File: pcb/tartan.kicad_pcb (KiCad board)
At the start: 2 copper layers, 285 x 117 mm, 165 parts, among them J1 AVR_ISP_6, J3 Conn_01x01_Pin, J4 USB_OTG, SW1 SW_Push, SW10 SW_Push, SW11 SW_Push, SW12 SW_Push, SW13 SW_Push, SW14 SW_Push, SW15 SW_Push, SW16 SW_Push, SW17 SW_Push, SW18 SW_Push, SW19 SW_Push, SW2 SW_Push, SW20 SW_Push, SW21 SW_Push, SW22 SW_Push, SW23 SW_Push, SW24 SW_Push, SW25 SW_Push, SW26 SW_Push, SW27 SW_Push, SW28 SW_Push, SW29 SW_Push, SW3 SW_Push, SW30 SW_Push, SW31 SW_Push, SW32 SW_Push, SW33 SW_Push, SW34 SW_Push, SW35 SW_Push, SW36 SW_Push, SW37 SW_Push, SW38 SW_Push, SW39 SW_Push, SW4 SW_Push, SW40 SW_Push, SW41 SW_Push, SW42 SW_Push, SW43 SW_Push, SW44 SW_Push, SW45 SW_Push, SW46 SW_Push, SW47 SW_Push, SW48 SW_Push, SW49 SW_Push, SW5 SW_Push, SW50 SW_Push, SW51 SW_Push, SW52 SW_Push, SW53 SW_Push, SW54 SW_Push, SW55 SW_Push, SW56 SW_Push, SW57 SW_Push, SW58 SW_Push, SW59 SW_Push, SW6 SW_Push, SW60 SW_Push, SW61 SW_Push, SW62 SW_Push, SW63 SW_Push, SW64 SW_Push, SW65 SW_Push, SW66 SW_Push, SW67 SW_Push, SW68 SW_Push, SW69 SW_Push, SW7 SW_Push, SW70 RESET, SW71 BOOT, SW8 SW_Push, SW9 SW_Push, U1 ATMEGA328-PU, Y1 16MHz

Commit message: Added stabilizers back and hopefully fixed a bunch of issues (tm).
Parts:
- added STAB1: 2U, tartan:STAB_MX_2u, F.Cu at (295.9, 61.1)
- added STAB2: 2U, tartan:STAB_MX_2u, F.Cu at (303.7, 90.6)
- added STAB3: 2U, tartan:STAB_MX_2u, F.Cu at (288.9, 119.7)
- added STAB4: 2U, tartan:STAB_MX_2u, F.Cu at (293.6, 99.6)
- added STAB5: 2U, tartan:STAB_MX_2u, F.Cu at (51.4, 118.4)
- added STAB6: 6.25u, tartan:STAB_MX_6.25u, F.Cu at (160.6, 137.5)
- moved TH1 0.27 mm to (273.8, 48.1)
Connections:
- net Net-(D65-K) renamed /D+
- net Net-(D66-K) renamed /D-
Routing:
- net GND: track 2.54 -> 6.25 mm, vias 51 -> 55
- net /ROW1: track 215.8 -> 217.3 mm
- net Net-(D56-A): track 180.2 -> 181.4 mm
- net /COL9: track 172.8 -> 173.6 mm

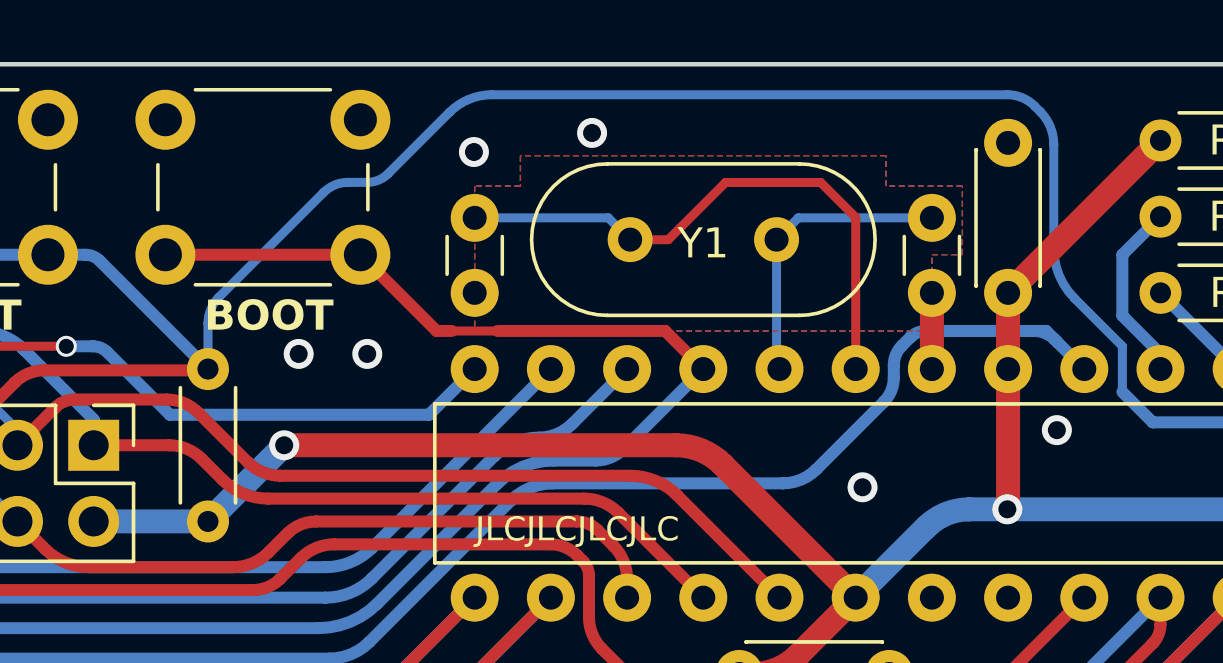
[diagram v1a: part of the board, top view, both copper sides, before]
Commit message: Added render pipeline to have screenshots.
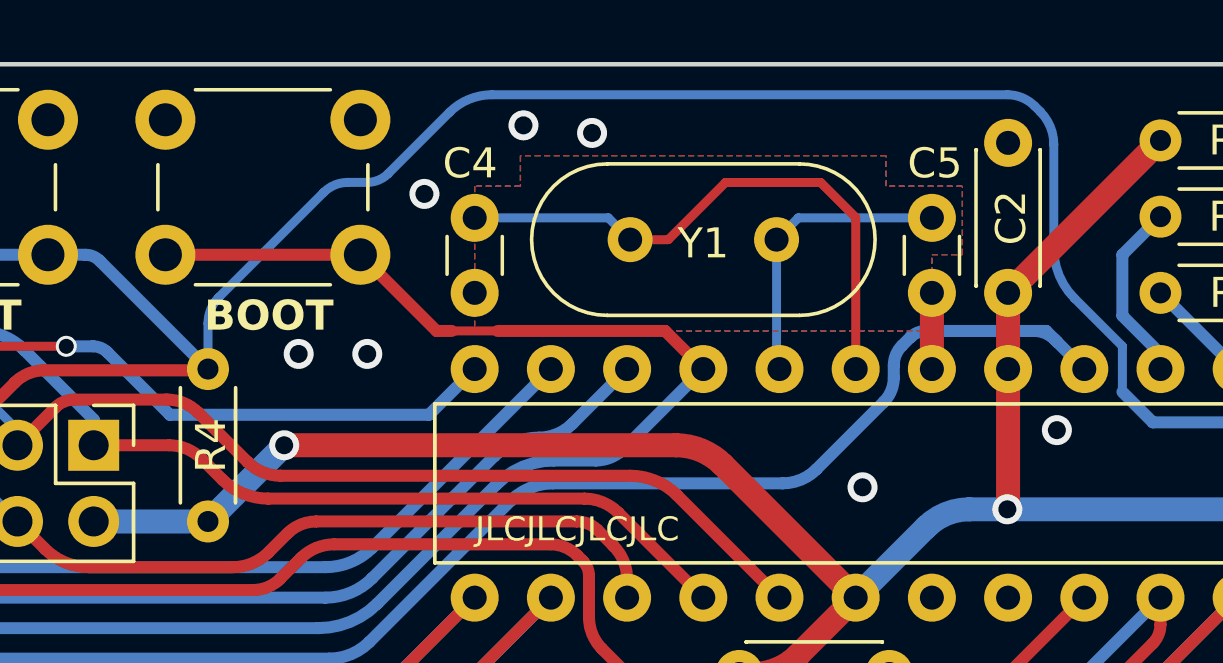
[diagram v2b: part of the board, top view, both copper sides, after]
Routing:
- net GND: vias 55 -> 56
